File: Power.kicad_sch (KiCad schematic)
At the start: 35 parts, among them Q1 TIP35C, SW2 POWER SWITCH, U2 LM7815C

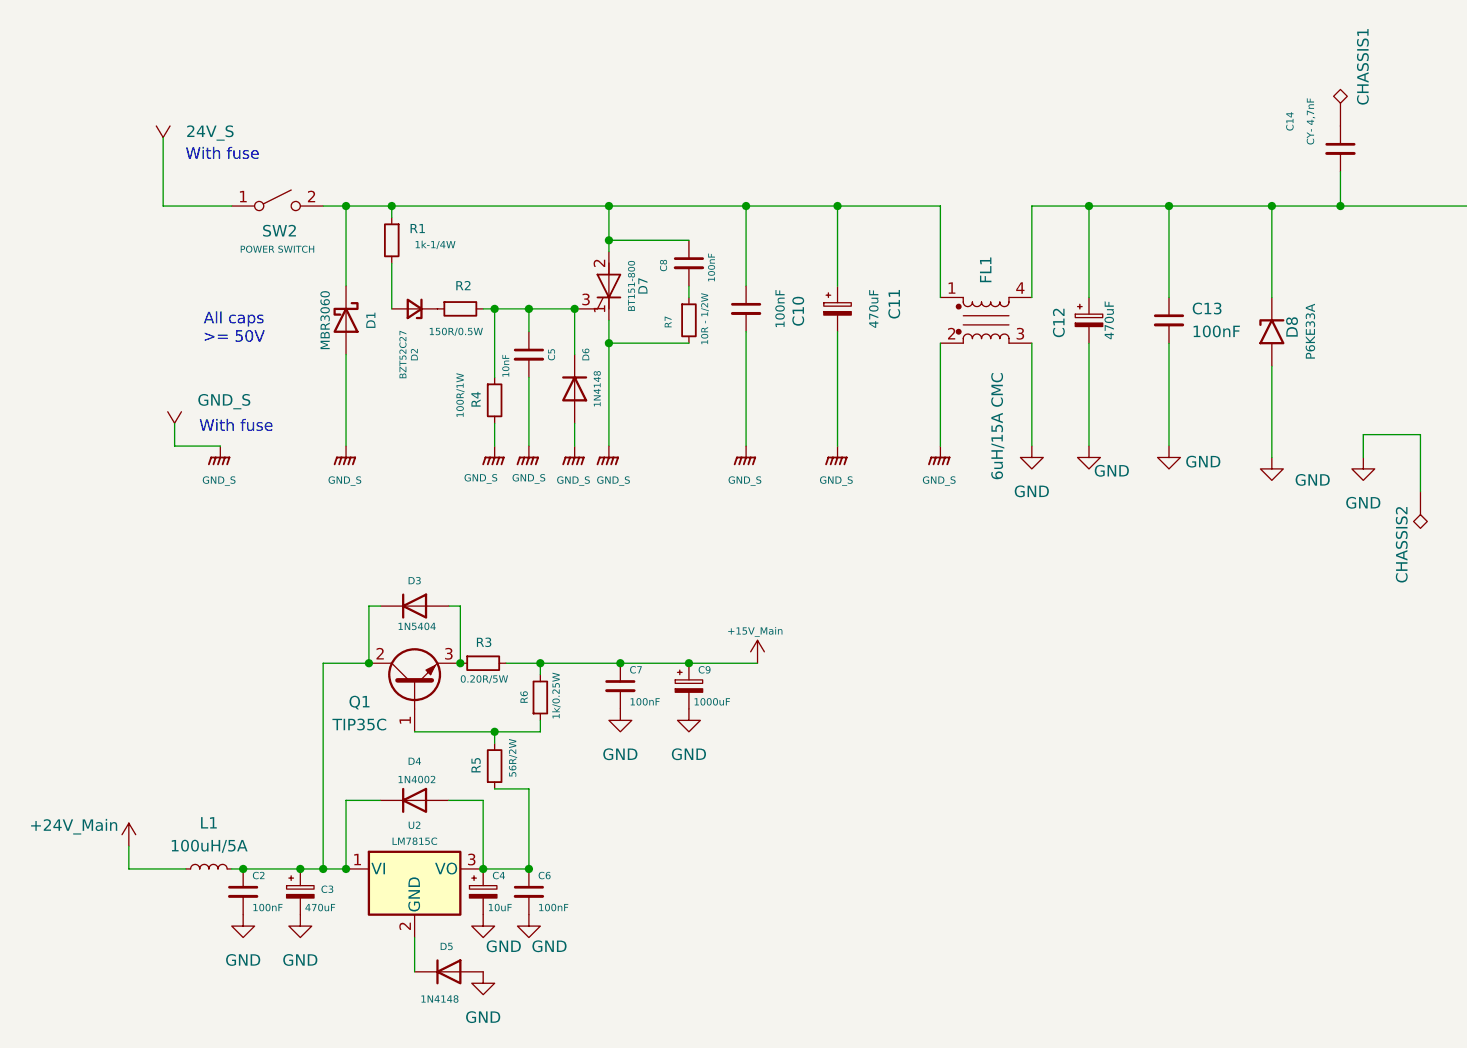
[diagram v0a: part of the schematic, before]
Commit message: Resistive adder of mixers
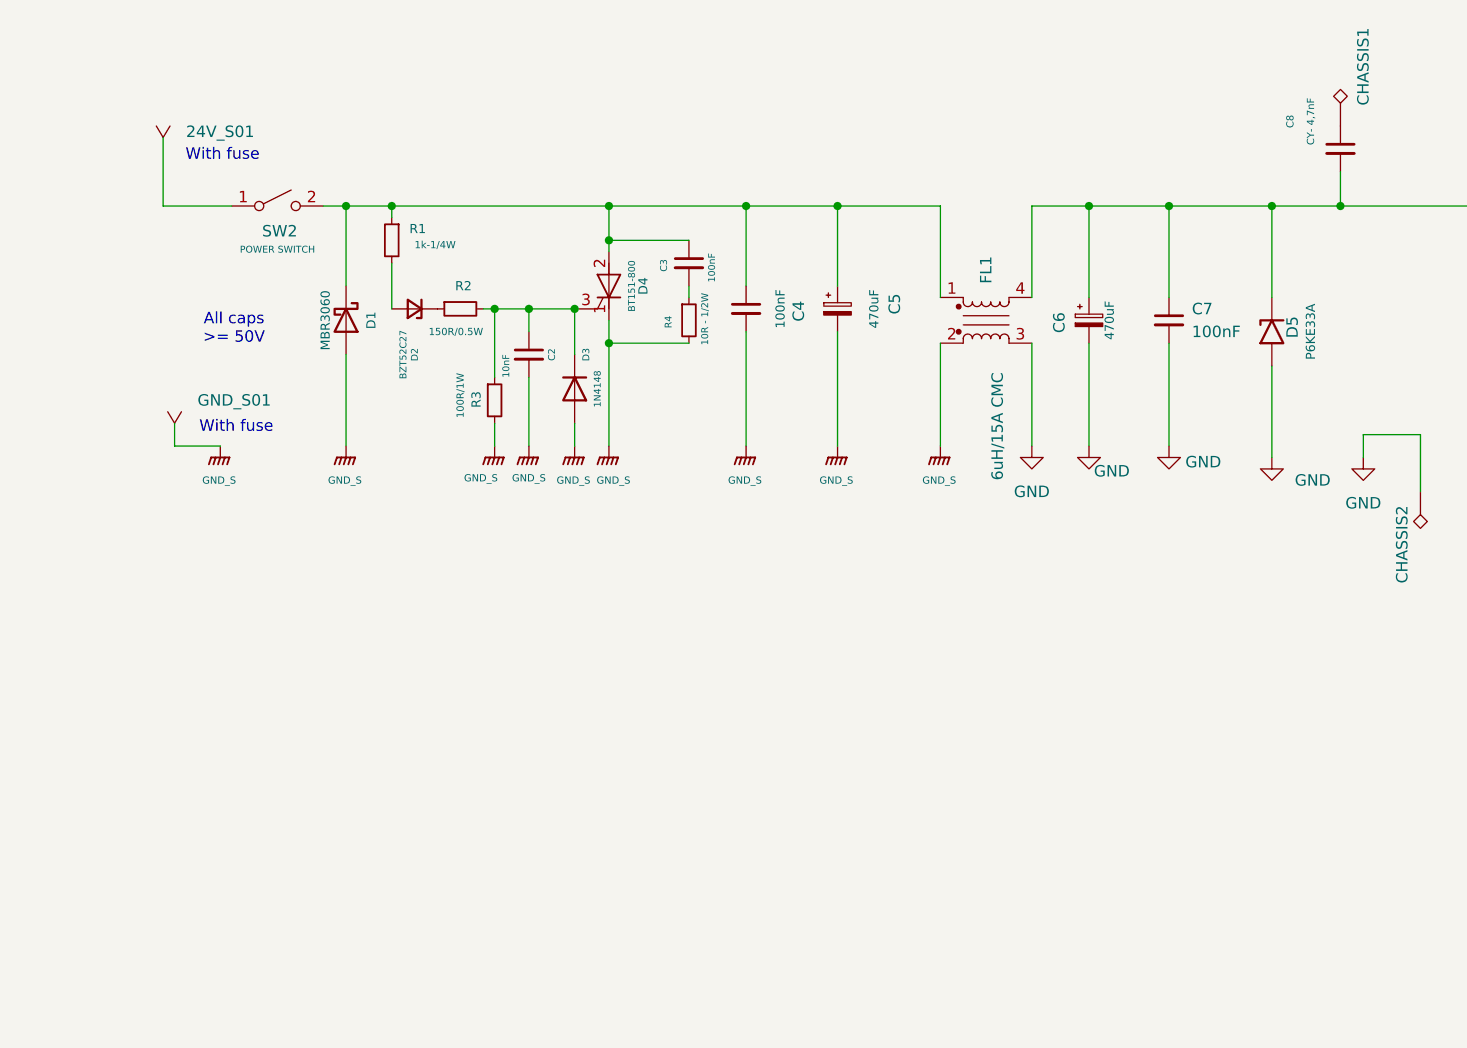
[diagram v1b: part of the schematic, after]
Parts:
- removed C2, C6, C7: 100nF, symbol Device:C_Small
- removed C3: 470uF, symbol Device:C_Polarized_Small
- removed C4: 10uF, symbol Device:C_Polarized_Small
- removed C9: 1000uF, symbol Device:C_Polarized_Small
- removed D3: 1N5404, Diode_THT:D_DO-201AD_P15.24mm_Horizontal, symbol Diode:1N5404
- removed D4: 1N4002, Diode_THT:D_DO-41_SOD81_P10.16mm_Horizontal, symbol Diode:1N4002
- removed D5: 1N4148, Diode_THT:D_DO-35_SOD27_P7.62mm_Horizontal, symbol Diode:1N4148
- removed L1: 100uH/5A, symbol Device:L_Small
- removed Q1: TIP35C, Package_TO_SOT_THT:TO-247-3_Vertical, symbol Transistor_BJT:TIP3055G
- removed R3: 0.20R/5W, symbol Device:R_Small
- removed R5: 56R/2W, symbol Device:R_Small
- removed R6: 1k/0.25W, symbol Device:R_Small
- removed U2: LM7815C, Package_TO_SOT_THT:TO-220-3_Vertical, symbol Regulator_Linear:LM7815_TO220
- renumbered C5 to C2, C8 to C3, C10 to C4, C11 to C5, C12 to C6, C13 to C7, C14 to C8, D6 to D3, D7 to D4, D8 to D5, R4 to R3, R7 to R4

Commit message: Power work
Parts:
- added C83, C86, C88, C91, C93, C96: 100nF, symbol Device:C_Small
- added C84, C85, C89, C90, C94, C95: 470uF, symbol Device:C_Polarized_Small
- added C87, C92, C97: CY- 4,7nF, symbol Device:C_Small
- added CHASSIS3, CHASSIS4, CHASSIS5, CHASSIS6, CHASSIS7, CHASSIS8: TestPoint_Alt, symbol Connector:TestPoint_Alt
- added D16: P6KE15A, Diode_THT:D_P600_R-6_P20.00mm_Horizontal, symbol Diode:5KPxxA
- added D17: P6KE6.8A, Diode_THT:D_P600_R-6_P20.00mm_Horizontal, symbol Diode:5KPxxA
- added D18: SMBJ3.3A, Diode_THT:D_P600_R-6_P20.00mm_Horizontal, symbol Diode:5KPxxA
- added FL2, FL3, FL4: 6uH/1A CMC, Inductor_THT:L_CommonMode_PulseElectronics_PH9455x105NL_1, symbol Filter:Choke_CommonMode_PulseElectronics_PH9455x105NL
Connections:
- net GND: now also C85.2, C86.2, C90.2, C91.2, C95.2, C96.2, CHASSIS4.1, CHASSIS6.1, CHASSIS8.1, D16.2 (A2), D17.2 (A2), D18.2 (A2), FL2.3, FL3.3, FL4.3
- net GND_S renamed GND_PS
- net GND_PS: no longer SW2.1 (A)
- new net: C97.1, CHASSIS7.1
- new net: C87.1, CHASSIS3.1
- new net: C92.1, CHASSIS5.1
- new net +12V_ATX: C83.1, C84.1, FL2.1
- new net +12V_MAIN: C85.1, C86.1, C87.2, D16.1 (A1), FL2.4
- new net +24V: SW2.1 (A)
- new net +3.3V_ATX: C93.1, C94.1, FL4.1
- new net +3.3V_MAIN: C95.1, C96.1, C97.2, D18.1 (A1), FL4.4
- new net +5V_ATX: C88.1, C89.1, FL3.1
- new net +5V_MAIN: C90.1, C91.1, C92.2, D17.1 (A1), FL3.4
- new net GND_ATX: C83.2, C84.2, C88.2, C89.2, C93.2, C94.2, FL2.2, FL3.2, FL4.2

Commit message: BPF Work 2
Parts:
- renumbered C91 to C10, C85 to C11, C5 to C12, C86 to C13, C92 to C14, C87 to C15, C6 to C16, C7 to C17, C8 to C18, C93 to C19, C88 to C2, C94 to C20, C95 to C21, C96 to C22, C97 to C23, C89 to C3, C83 to C4, C2 to C5, C84 to C6, C90 to C7, C3 to C8, C4 to C9, CHASSIS5 to CHASSIS1, CHASSIS6 to CHASSIS2, CHASSIS1 to CHASSIS5, CHASSIS2 to CHASSIS6, D17 to D5, D16 to D6, D5 to D7, D18 to D8, FL3 to FL1, FL1 to FL3
